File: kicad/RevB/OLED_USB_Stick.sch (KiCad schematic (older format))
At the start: 0 parts

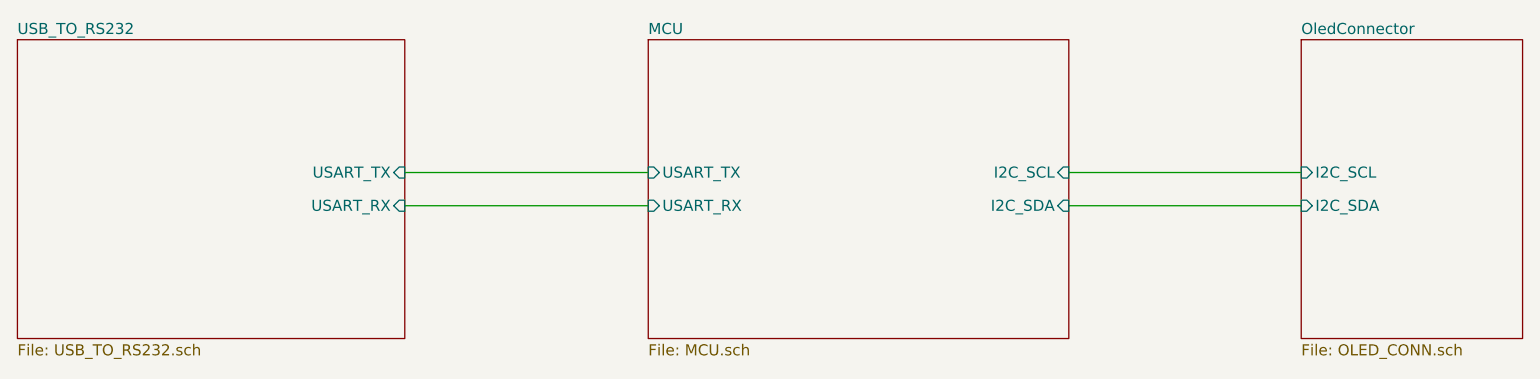
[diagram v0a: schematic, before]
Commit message: updated hw
- corrected i2c pins
- changed reset btn to horizontal mount
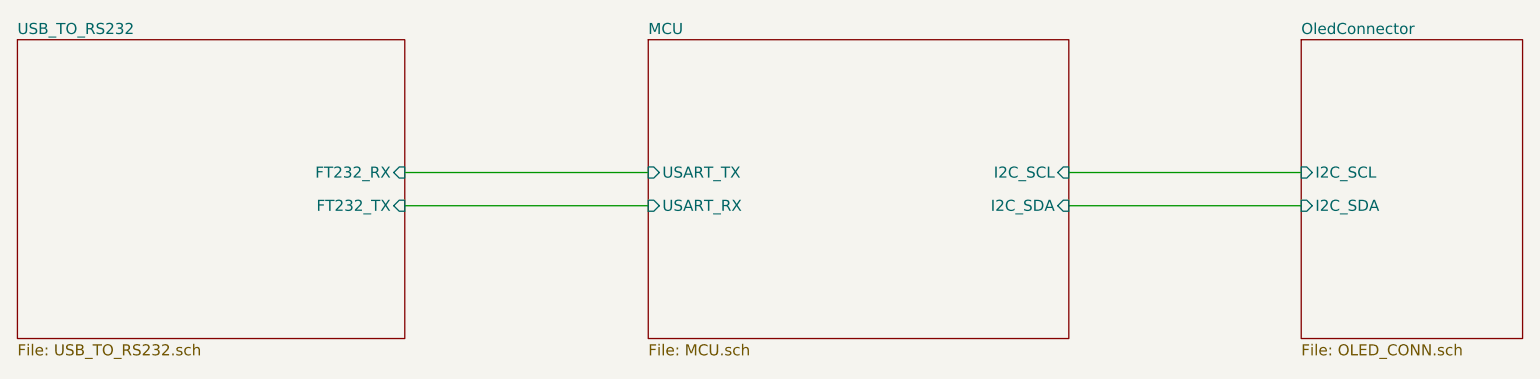
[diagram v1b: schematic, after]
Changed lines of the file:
@@
 $EndDescr
-$Sheet
-S 2300 2700 1750 1350
-U 5F6D964E
-F0 "USB_TO_RS232" 50
-F1 "USB_TO_RS232.sch" 50
-F2 "USART_TX" I R 4050 3300 50
-F3 "USART_RX" I R 4050 3450 50
-$EndSheet
 $Sheet
 S 5150 2700 1900 1350
@@
 F5 "USART_RX" I L 5150 3450 50
 $EndSheet
-Wire Wire Line
-	5150 3300 4050 3300
-Wire Wire Line
-	4050 3450 5150 3450
 $Sheet
 S 8100 2700 1000 1350
@@
 Wire Wire Line
 	8100 3450 7050 3450
+Wire Wire Line
+	4050 3450 5150 3450
+$Sheet
+S 2300 2700 1750 1350
+U 5F6D964E
+F0 "USB_TO_RS232" 50
+F1 "USB_TO_RS232.sch" 50
+F2 "FT232_RX" I R 4050 3300 50
+F3 "FT232_TX" I R 4050 3450 50
+$EndSheet
+Wire Wire Line
+	5150 3300 4050 3300
 $EndSCHEMATC
